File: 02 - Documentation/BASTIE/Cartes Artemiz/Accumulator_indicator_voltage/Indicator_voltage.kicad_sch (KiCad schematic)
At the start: 37 parts, among them IC1 Contrôleur LT8316EFE#PBF, J7 2P Droit 2-11-2022, Q1 NMOS SQ2348ES-T1_GE3, Q2 NMOS TK3P80E_RQ, U1 Alim LP TSR_0.5-2450

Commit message: Routage Voltage Indicator
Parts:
- removed C11: 10u, EPSA:CAPC2012X130N, symbol EPSA_lib:Condensateur 0805Y1000104JXT
- C10: footprint EPSA:CAPC2012X130N -> EPSA_lib:CAPC2012X130N
- C6: footprint EPSA_lib:CAPC2012X130N -> GRM31x; symbol EPSA_lib:Condensateur 0805Y1000104JXT -> EPSA_lib:Condensateur GRM31CR71E106KA12L; Height 1.3 -> 1.15; Manufacturer_Name Syfer -> Murata Electronics; Manufacturer_Part_Number 0805Y1000104JXT -> GRM31CR71E106KA12L; Mouser Part Number (none) -> 81-GRM31CR71E106KA12; Mouser Price/Stock (none) -> https://www.mouser.co.uk/ProductDetail/Murata-Electronics/G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
- L1: footprint WE-PD_1260/1245/1280/121054 -> WE-PD_1260_1245_1280_121054
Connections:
- net +5V: now also C10.2
- net HV in: now reaches F1.1, TP1.1

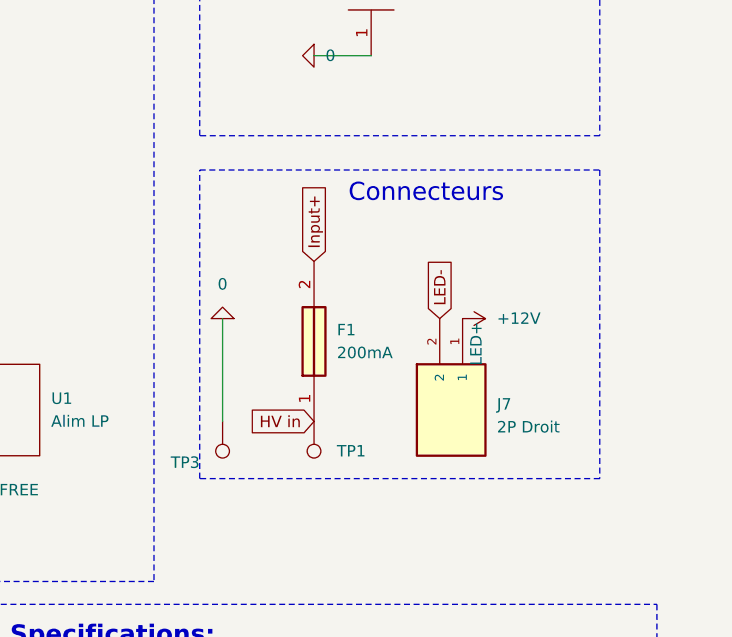
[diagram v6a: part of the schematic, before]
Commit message: Ajout compo convertisseur 600V + IMD SCS + BOM AIR
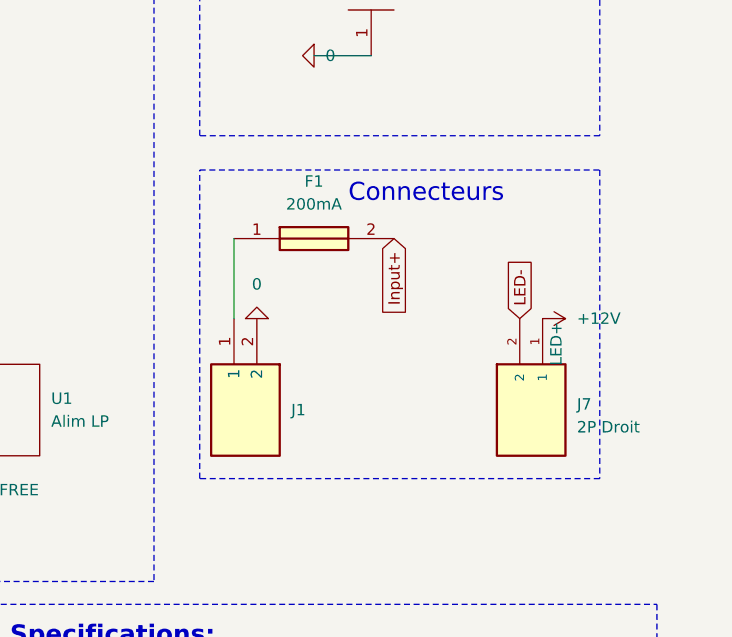
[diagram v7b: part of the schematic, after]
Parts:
- removed TP1, TP3: ${SIM.PARAMS}, Connector_Wire:SolderWire-2.5sqmm_1x01_D2.4mm_OD3.6mm, symbol EPSA_lib:TestPoint
- added J1: 2P Angle HV 200241-1212, 2002411212, symbol EPSA_lib:2P Angle HV 200241-1212
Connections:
- net 0: now also J1.2
- net HV in: no longer names the net of F1.1
- net HV in: now also J1.1
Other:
- moved on the sheet: J7
